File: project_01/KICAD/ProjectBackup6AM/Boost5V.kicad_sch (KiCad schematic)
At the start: 28 parts, among them U1 TPB4056A20-ES1R, U2 DRV5032FADBZR, U3 TPS613222ADBVR, U5 XC6206P332MR-G

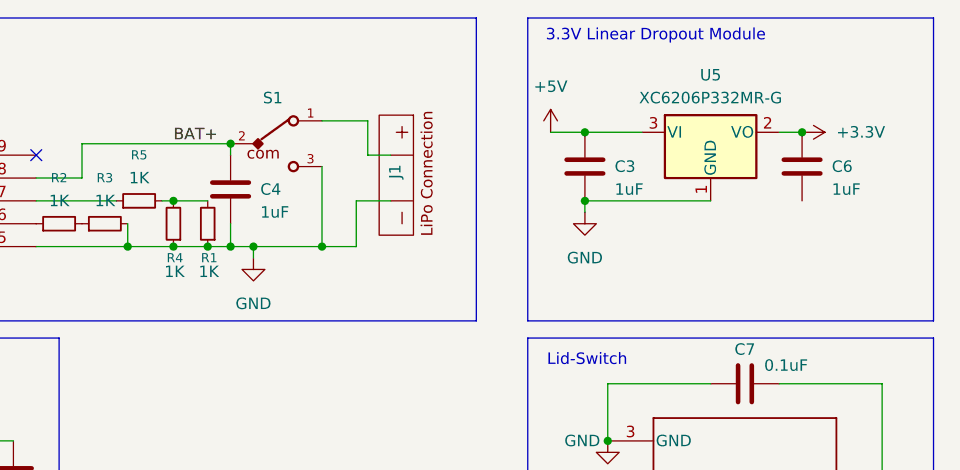
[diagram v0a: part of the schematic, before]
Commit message: Update KiCad schematics to v10; clean backups
Bump KiCad schematic version/generator to v10 and normalize symbol/property metadata in Boost5V.kicad_sch (add show_name/do_not_autoplace/hide/in_pos_files, standardize pin names/numbers/types and orientations). Apply similar component property adjustments (e.g. TPB4056, XC6206, TPS613222) and update related project PCB/PRO/PRL/SCH files. Add ProjectBackupFINAL and several new zip backups, and remove many old backup, cache and lock files to clean up the repository. These are primarily metadata and housekeeping changes, not functional circuit edits.
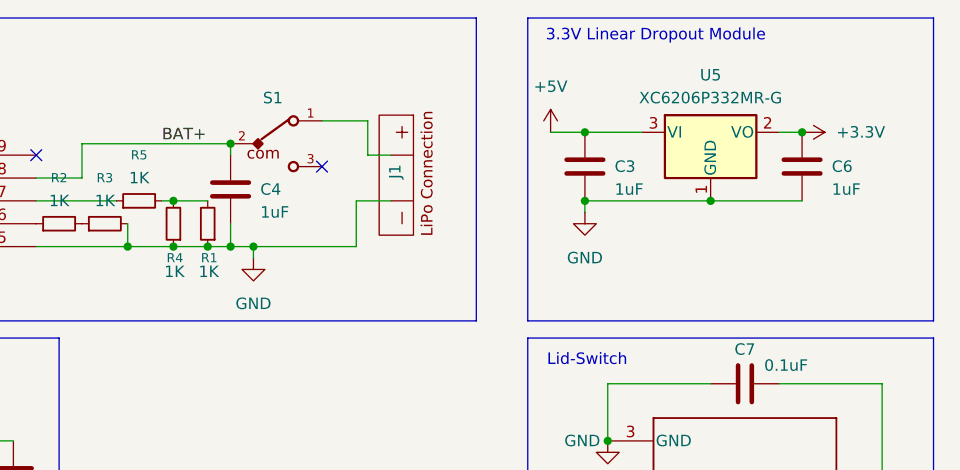
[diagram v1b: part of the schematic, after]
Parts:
- J1, S1: value ~ -> (none)
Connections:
- net GND: now also C6.2; no longer S1.3
- no-connect marks 1 -> 2
